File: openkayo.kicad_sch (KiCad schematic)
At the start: 4 parts

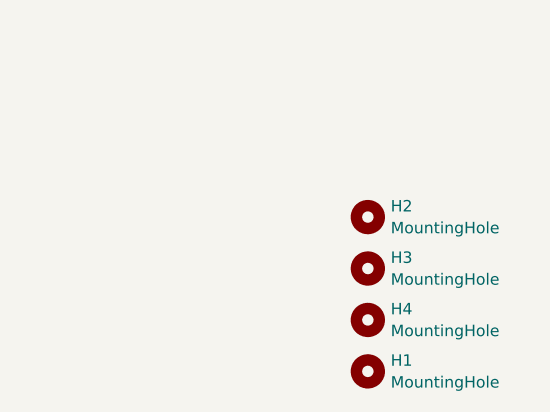
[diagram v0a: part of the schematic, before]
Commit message: Update to KiCad 8.
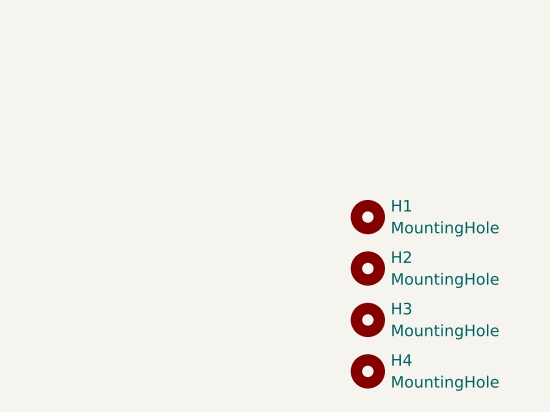
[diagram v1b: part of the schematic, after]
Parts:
- renumbered H2 to H1, H3 to H2, H4 to H3, H1 to H4
